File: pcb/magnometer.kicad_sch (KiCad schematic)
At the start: 7 parts, among them U21 QMC5883L

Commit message: Remove sensor hub
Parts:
- renumbered C23 to C43, C24 to C44, C25 to C45, C26 to C46, R37 to R31, R38 to R32
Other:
- moved on the sheet: C43, C44, C45

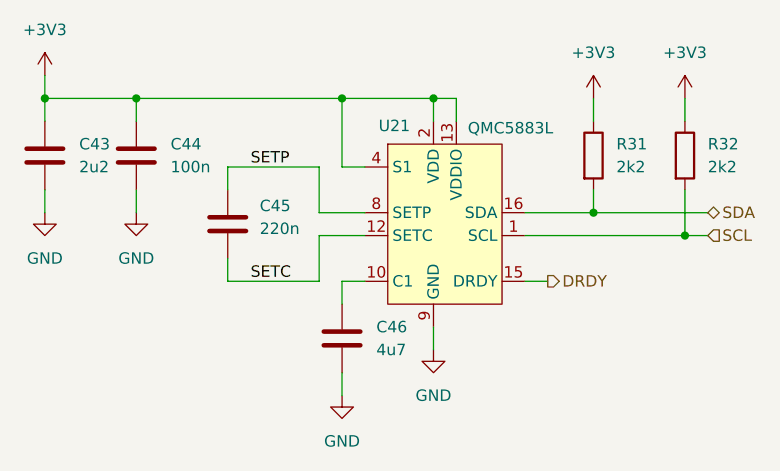
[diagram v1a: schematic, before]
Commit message: Finish schematic
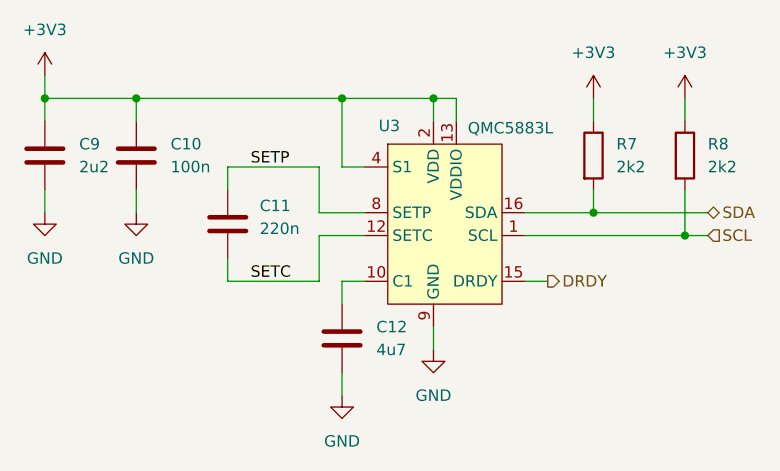
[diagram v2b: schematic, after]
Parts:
- renumbered C44 to C10, C45 to C11, C46 to C12, C43 to C9, R31 to R7, R32 to R8, U21 to U3
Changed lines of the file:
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@@
 		(dnp no)
 		(fields_autoplaced yes)
-		(property "Reference" "#PWR0160"
+		(property "Reference" "#PWR041"
 			(at 93.98 80.01 0)
 			(effects
@@
 			(project "raven"
 				(path "/38b0a34b-2047-47f6-90d7-ccdf77e8e212/bb55d5dc-17ea-4c4f-8b20-038db2561a4a"
-					(reference "#PWR0281")
+					(reference "#PWR041")
 					(unit 1)
 				)
@@
 		(dnp no)
 		(fields_autoplaced yes)
-		(property "Reference" "R32"
+		(property "Reference" "R8"
 			(at 124.46 50.7999 0)
 			(effects
@@
 			(project "raven"
 				(path "/38b0a34b-2047-47f6-90d7-ccdf77e8e212/bb55d5dc-17ea-4c4f-8b20-038db2561a4a"
-					(reference "R86")
+					(reference "R8")
 					(unit 1)
 				)
@@
 		(dnp no)
 		(fields_autoplaced yes)
-		(property "Reference" "#PWR0156"
+		(property "Reference" "#PWR037"
 			(at 50.8 46.99 0)
 			(effects
@@
 			(project "raven"
 				(path "/38b0a34b-2047-47f6-90d7-ccdf77e8e212/bb55d5dc-17ea-4c4f-8b20-038db2561a4a"
-					(reference "#PWR0277")
+					(reference "#PWR037")
 					(unit 1)
 				)
@@
 		(dnp no)
 		(fields_autoplaced yes)
-		(property "Reference" "#PWR0159"
+		(property "Reference" "#PWR040"
 			(at 83.82 85.09 0)
 			(effects
@@
 			(project "raven"
 				(path "/38b0a34b-2047-47f6-90d7-ccdf77e8e212/bb55d5dc-17ea-4c4f-8b20-038db2561a4a"
-					(reference "#PWR0280")
+					(reference "#PWR040")
 					(unit 1)
 				)
@@
 		(dnp no)
 		(fields_autoplaced yes)
-		(property "Reference" "#PWR0158"
+		(property "Reference" "#PWR039"
 			(at 60.96 64.77 0)
 			(effects
@@
 			(project "raven"
 				(path "/38b0a34b-2047-47f6-90d7-ccdf77e8e212/bb55d5dc-17ea-4c4f-8b20-038db2561a4a"
-					(reference "#PWR0279")
+					(reference "#PWR039")
 					(unit 1)
 				)
@@
 		(dnp no)
 		(fields_autoplaced yes)
-		(property "Reference" "#PWR0161"
+		(property "Reference" "#PWR042"
 			(at 111.76 49.53 0)
 			(effects
@@
 			(project "raven"
 				(path "/38b0a34b-2047-47f6-90d7-ccdf77e8e212/bb55d5dc-17ea-4c4f-8b20-038db2561a4a"
-					(reference "#PWR0282")
+					(reference "#PWR042")
 					(unit 1)
 				)
@@
 		(dnp no)
 		(fields_autoplaced yes)
-		(property "Reference" "C43"
+		(property "Reference" "C9"
 			(at 54.61 50.7999 0)
 			(effects
@@
 			(project "raven"
 				(path "/38b0a34b-2047-47f6-90d7-ccdf77e8e212/bb55d5dc-17ea-4c4f-8b20-038db2561a4a"
-					(reference "C23")
+					(reference "C9")
 					(unit 1)
 				)
@@
 		(dnp no)
 		(fields_autoplaced yes)
-		(property "Reference" "C46"
+		(property "Reference" "C12"
 			(at 87.63 71.1199 0)
 			(effects
@@
 			(project "raven"
 				(path "/38b0a34b-2047-47f6-90d7-ccdf77e8e212/bb55d5dc-17ea-4c4f-8b20-038db2561a4a"
-					(reference "C26")
+					(reference "C12")
 					(unit 1)
 				)
@@
 		(dnp no)
 		(fields_autoplaced yes)
-		(property "Reference" "#PWR0162"
+		(property "Reference" "#PWR043"
 			(at 121.92 49.53 0)
 			(effects
@@
 			(project "raven"
 				(path "/38b0a34b-2047-47f6-90d7-ccdf77e8e212/bb55d5dc-17ea-4c4f-8b20-038db2561a4a"
-					(reference "#PWR0283")
+					(reference "#PWR043")
 					(unit 1)
 				)
@@
 		(on_board yes)
 		(dnp no)
-		(property "Reference" "U21"
+		(property "Reference" "U3"
 			(at 87.884 48.768 0)
 			(effects
@@
 			(project "raven"
 				(path "/38b0a34b-2047-47f6-90d7-ccdf77e8e212/bb55d5dc-17ea-4c4f-8b20-038db2561a4a"
-					(reference "U35")
+					(reference "U3")
 					(unit 1)
 				)
@@
 		(dnp no)
 		(fields_autoplaced yes)
-		(property "Reference" "R31"
+		(property "Reference" "R7"
 			(at 114.3 50.7999 0)
 			(effects
@@
 			(project "raven"
 				(path "/38b0a34b-2047-47f6-90d7-ccdf77e8e212/bb55d5dc-17ea-4c4f-8b20-038db2561a4a"
-					(reference "R85")
+					(reference "R7")
 					(unit 1)
 				)
@@
 		(on_board yes)
 		(dnp no)
-		(property "Reference" "C45"
+		(property "Reference" "C11"
 			(at 74.676 57.658 0)
 			(effects
@@
 			(project "raven"
 				(path "/38b0a34b-2047-47f6-90d7-ccdf77e8e212/bb55d5dc-17ea-4c4f-8b20-038db2561a4a"
-					(reference "C25")
+					(reference "C11")
 					(unit 1)
 				)
@@
 		(dnp no)
 		(fields_autoplaced yes)
-		(property "Reference" "C44"
+		(property "Reference" "C10"
 			(at 64.77 50.7999 0)
 			(effects
@@
 			(project "raven"
 				(path "/38b0a34b-2047-47f6-90d7-ccdf77e8e212/bb55d5dc-17ea-4c4f-8b20-038db2561a4a"
-					(reference "C24")
+					(reference "C10")
 					(unit 1)
 				)
@@
 		(dnp no)
 		(fields_autoplaced yes)
-		(property "Reference" "#PWR0157"
+		(property "Reference" "#PWR038"
 			(at 50.8 64.77 0)
 			(effects
@@
 			(project "raven"
 				(path "/38b0a34b-2047-47f6-90d7-ccdf77e8e212/bb55d5dc-17ea-4c4f-8b20-038db2561a4a"
-					(reference "#PWR0278")
-					(unit 1)
-				)
+					(reference "#PWR038")
+					(unit 1)
+				)

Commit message: Save progress
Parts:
- R7, R8: value 2k2 -> 10k; LCSC C25879 -> C25744
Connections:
- net C1: now reaches C12.1, U3.10 (C1)
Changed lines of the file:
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@@
 		)
 	)
-	(label "SETP"
-		(at 73.66 53.34 0)
+	(label "C1"
+		(at 83.82 66.04 0)
 		(fields_autoplaced yes)
 		(effects
@@
 		)
 	)
-	(label "SETC"
-		(at 73.66 66.04 0)
+	(label "SETP"
+		(at 73.66 53.34 0)
 		(fields_autoplaced yes)
 		(effects
@@
 		)
 	)
+	(label "SETC"
+		(at 73.66 66.04 0)
+		(fields_autoplaced yes)
+		(effects
+			(font
+				(size 1.27 1.27)
+			)
+			(justify left bottom)
+		)
+	)
 	(hierarchical_label "DRDY"
 		(shape output)
@@
 	)
 	(symbol
+		(lib_id "Device:R")
+		(at 121.92 52.07 0)
+		(unit 1)
+		(exclude_from_sim no)
+		(in_bom yes)
+		(on_board yes)
+		(dnp no)
+		(fields_autoplaced yes)
+		(property "Reference" "R8"
+			(at 124.46 50.7999 0)
+			(effects
+				(font
+					(size 1.27 1.27)
+				)
+				(justify left)
+			)
+		)
+		(property "Value" "10k"
+			(at 124.46 53.3399 0)
+			(effects
+				(font
+					(size 1.27 1.27)
+				)
+				(justify left)
+			)
+		)
+		(property "Footprint" "Resistor_SMD:R_0402_1005Metric"
+			(at 120.142 52.07 90)
+			(effects
+				(font
+					(size 1.27 1.27)
+				)
+				(hide yes)
+			)
+		)
+		(property "Datasheet" "~"
+			(at 121.92 52.07 0)
+			(effects
+				(font
+					(size 1.27 1.27)
+				)
+				(hide yes)
+			)
+		)
+		(property "Description" "Resistor"
+			(at 121.92 52.07 0)
+			(effects
+				(font
+					(size 1.27 1.27)
+				)
+				(hide yes)
+			)
+		)
+		(property "LCSC" "C25744"
+			(at 121.92 52.07 0)
+			(effects
+				(font
+					(size 1.27 1.27)
+				)
+				(hide yes)
+			)
+		)
+		(pin "1"
+		)
+		(pin "2"
+		)
+		(instances
+			(project "raven"
+				(path "/38b0a34b-2047-47f6-90d7-ccdf77e8e212/bb55d5dc-17ea-4c4f-8b20-038db2561a4a"
+					(reference "R8")
+					(unit 1)
+				)
+			)
+		)
+	)
+	(symbol
 		(lib_id "power:GND")
 		(at 93.98 73.66 0)
@@
 	)
 	(symbol
-		(lib_id "Device:R")
-		(at 121.92 52.07 0)
-		(unit 1)
-		(exclude_from_sim no)
-		(in_bom yes)
-		(on_board yes)
-		(dnp no)
-		(fields_autoplaced yes)
-		(property "Reference" "R8"
-			(at 124.46 50.7999 0)
-			(effects
-				(font
-					(size 1.27 1.27)
-				)
-				(justify left)
-			)
-		)
-		(property "Value" "2k2"
-			(at 124.46 53.3399 0)
-			(effects
-				(font
-					(size 1.27 1.27)
-				)
-				(justify left)
-			)
-		)
-		(property "Footprint" "Resistor_SMD:R_0402_1005Metric"
-			(at 120.142 52.07 90)
-			(effects
-				(font
-					(size 1.27 1.27)
-				)
-				(hide yes)
-			)
-		)
-		(property "Datasheet" "~"
-			(at 121.92 52.07 0)
-			(effects
-				(font
-					(size 1.27 1.27)
-				)
-				(hide yes)
-			)
-		)
-		(property "Description" "Resistor"
-			(at 121.92 52.07 0)
-			(effects
-				(font
-					(size 1.27 1.27)
-				)
-				(hide yes)
-			)
-		)
-		(property "LCSC" "C25879"
-			(at 121.92 52.07 0)
-			(effects
-				(font
-					(size 1.27 1.27)
-				)
-				(hide yes)
-			)
-		)
-		(pin "1"
-		)
-		(pin "2"
-		)
-		(instances
-			(project "raven"
-				(path "/38b0a34b-2047-47f6-90d7-ccdf77e8e212/bb55d5dc-17ea-4c4f-8b20-038db2561a4a"
-					(reference "R8")
-					(unit 1)
-				)
-			)
-		)
-	)
-	(symbol
 		(lib_id "power:+3V3")
 		(at 50.8 43.18 0)
@@
 			)
 		)
-		(property "Value" "2k2"
+		(property "Value" "10k"
 			(at 114.3 53.3399 0)
 			(effects
@@
 			)
 		)
-		(property "LCSC" "C25879"
+		(property "LCSC" "C25744"
 			(at 111.76 52.07 0)
 			(effects

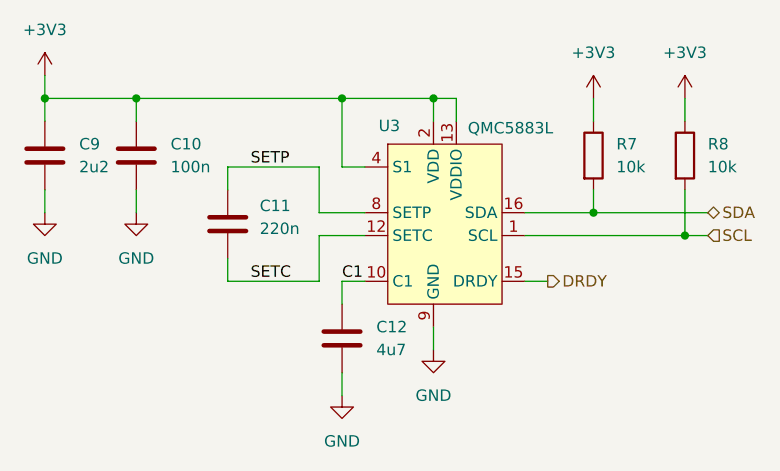
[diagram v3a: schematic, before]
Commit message: Finish schematic
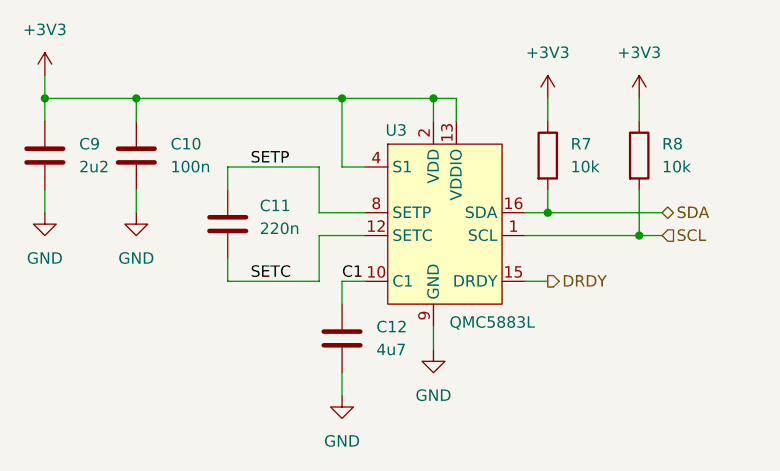
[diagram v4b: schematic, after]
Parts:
- removed U3: QMC5883L, Package_LGA:LGA-16_3x3mm_P0.5mm, symbol User_Symbols:QMC5883L
- added U3: QMC5883L, Package_LGA:LGA-16_3x3mm_P0.5mm, symbol Symbols:QMC5883L
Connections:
- net +3V3: now also U3.13 (VDDIO), U3.2 (VDD), U3.4 (S1)
- net C1: now also U3.10 (C1)
- net DRDY: now also U3.15 (DRDY)
- net GND: now also U3.11 (GND), U3.9 (GND)
- net SCL: now also U3.1 (SCL)
- net SDA: now also U3.16 (SDA)
- net SETC: now also U3.12 (SETC)
- net SETP: now also U3.8 (SETP)
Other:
- moved on the sheet: R7, R8

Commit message: Finish for revision 2 production
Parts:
- R7, R8: value 10k -> 7k5; LCSC C25744 -> C25918
- U3: now not fitted
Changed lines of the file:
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@@
 		(in_bom yes)
 		(on_board yes)
-		(dnp no)
+		(dnp yes)
 		(property "Reference" "U3"
 			(at 88.646 49.276 0)
@@
 			)
 		)
-		(property "Value" "10k"
+		(property "Value" "7k5"
 			(at 119.38 53.3399 0)
 			(effects
@@
 			)
 		)
-		(property "LCSC" "C25744"
+		(property "LCSC" "C25918"
 			(at 116.84 52.07 0)
 			(effects
@@
 			)
 		)
-		(property "Value" "10k"
+		(property "Value" "7k5"
 			(at 109.22 53.3399 0)
 			(effects
@@
 			)
 		)
-		(property "LCSC" "C25744"
+		(property "LCSC" "C25918"
 			(at 106.68 52.07 0)
 			(effects
